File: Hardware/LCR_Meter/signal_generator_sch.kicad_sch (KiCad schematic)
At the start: 0 parts

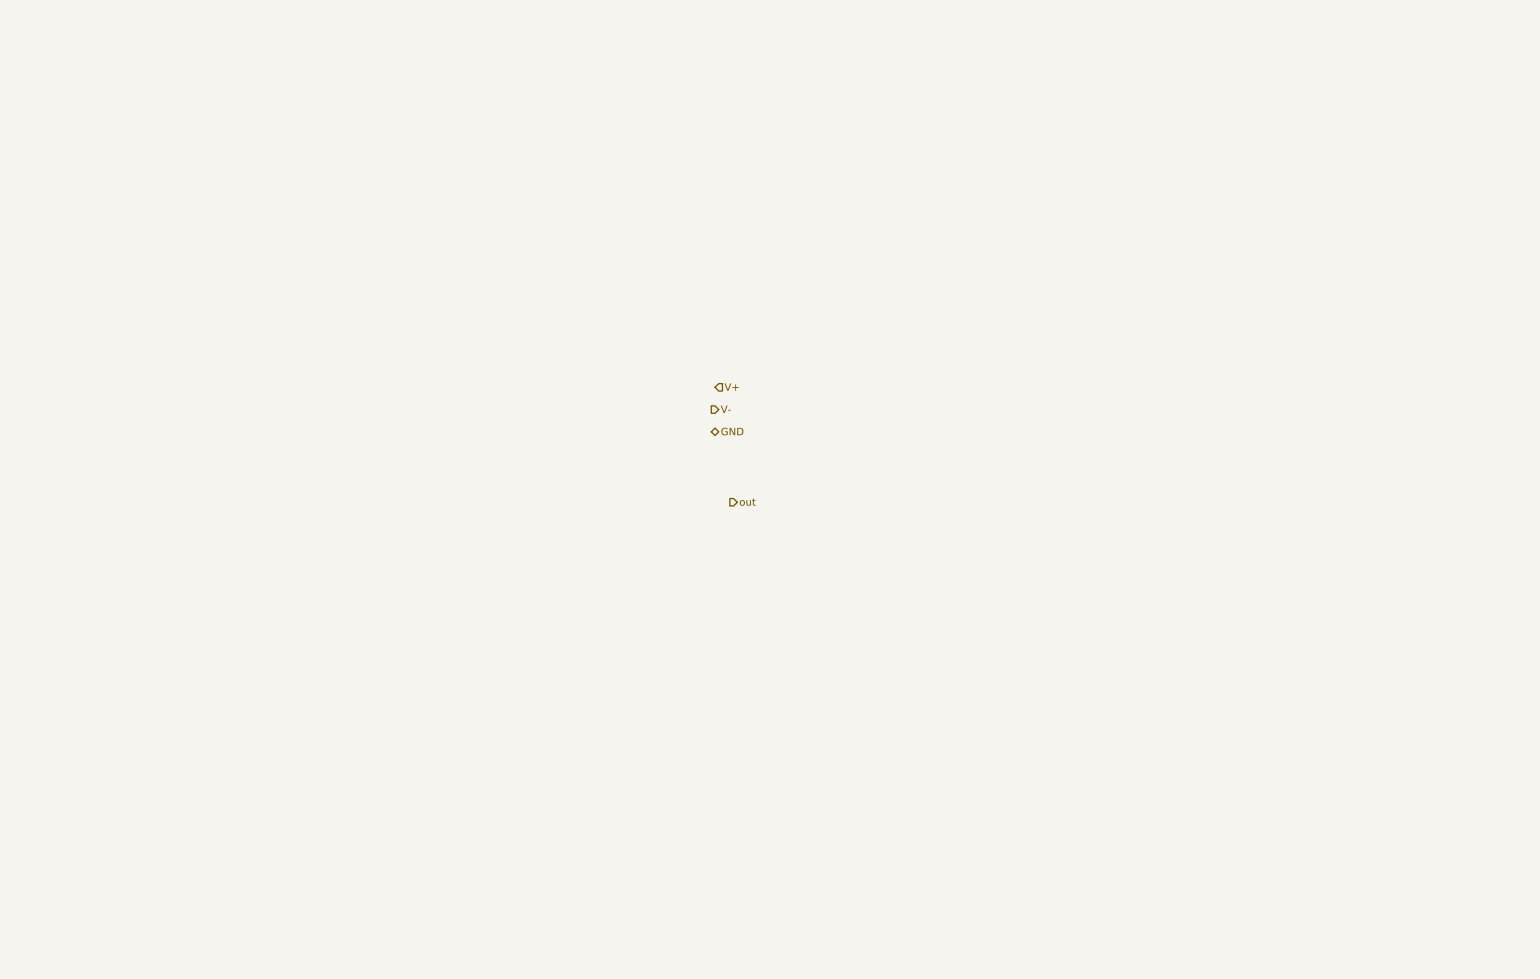
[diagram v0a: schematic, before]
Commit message: work on signal generator
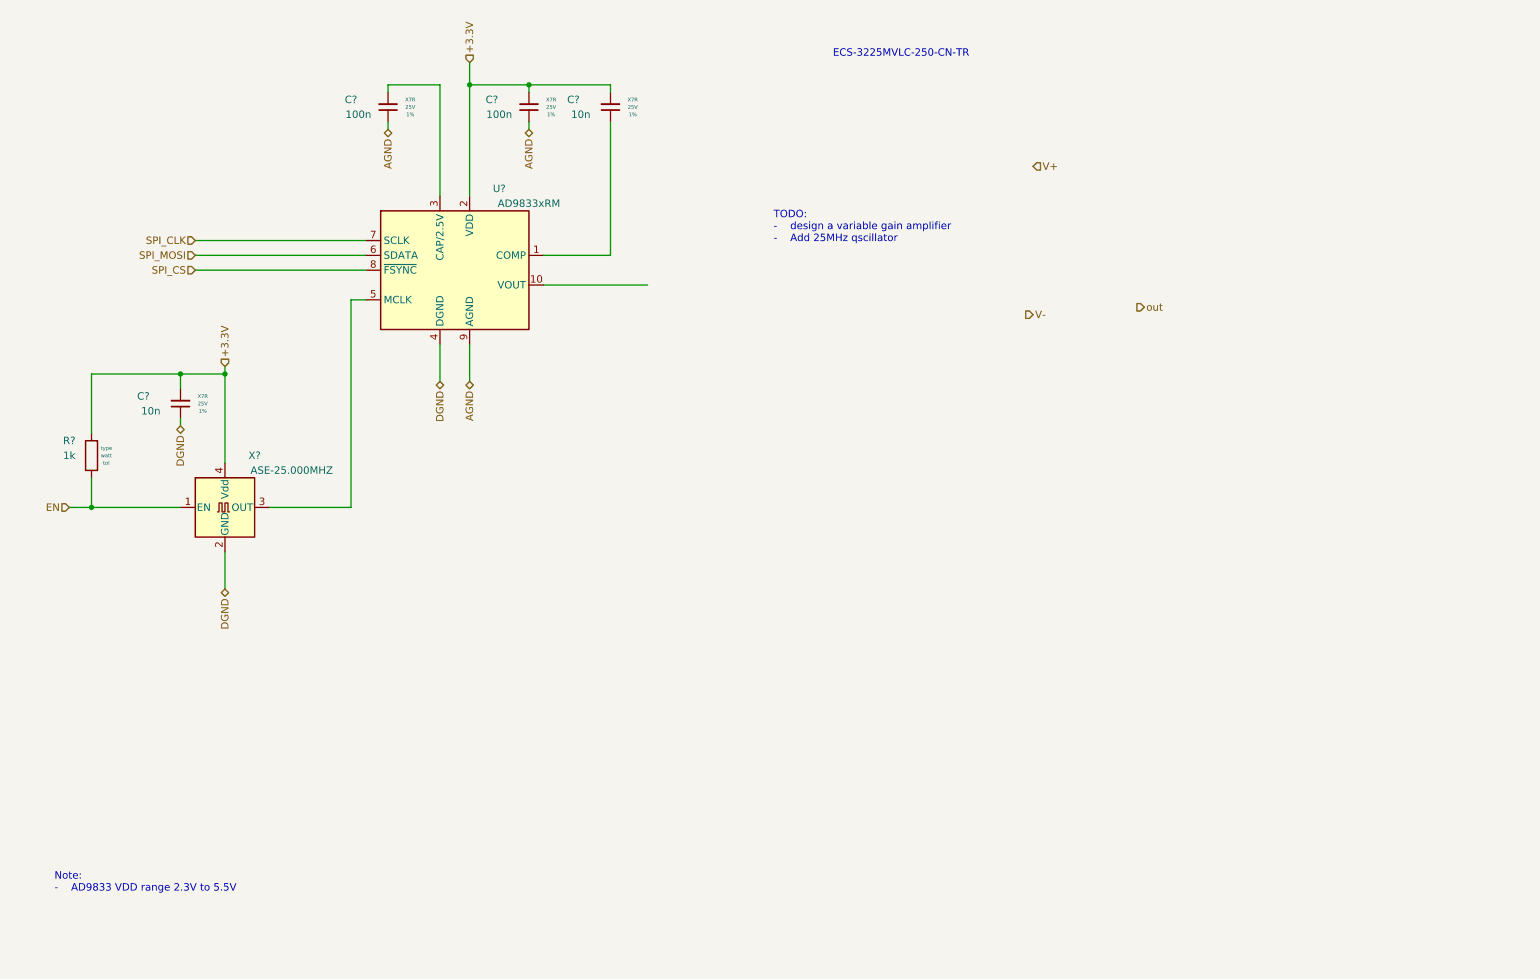
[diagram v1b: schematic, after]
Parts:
- added C? (x2): 100n, Capacitor_SMD:C_0805_2012Metric_Pad1.18x1.45mm_HandSolder, symbol 010_SMD_Capacitors:C_0805_hs
- added C? (x2): 10n, Capacitor_SMD:C_0805_2012Metric_Pad1.18x1.45mm_HandSolder, symbol 010_SMD_Capacitors:C_0805_hs
- added R?: 1k, Resistor_SMD:R_1206_3216Metric, symbol 000_SMD_Resitors:R_1206
- added U?: AD9833xRM, Package_SO:MSOP-10_3x3mm_P0.5mm, symbol Interface:AD9833xRM
- added X?: ASE-25.000MHZ, Oscillator:Oscillator_SMD_Abracon_ASE-4Pin_3.2x2.5mm, symbol Oscillator:ASE-xxxMHz
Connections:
- new net: C?.1, U?.1 (COMP)
- new net: C?.2, U?.3 (CAP/2.5V)
- new net: U?.5 (MCLK), X?.3 (OUT)
- new net +3.3V: C?.2, C?.2, C?.2, R?.2, U?.2 (VDD), X?.4 (Vdd)
- new net AGND: C?.1, C?.1, U?.9 (AGND)
- new net DGND: C?.1, U?.4 (DGND), X?.2 (GND)
- new net EN: R?.1, X?.1 (EN)
- new net SPI_CLK: U?.7 (SCLK)
- new net SPI_CS: U?.8 (~{FSYNC})
- new net SPI_MOSI: U?.6 (SDATA)
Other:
- note added: "ECS-3225MVLC-250-CN-TR"
- note added: "Note: - AD9833 VDD range 2.3V to 5.5V"
- note added: "TODO: - design a variable gain amplifier - Add 25MHz qscillator"

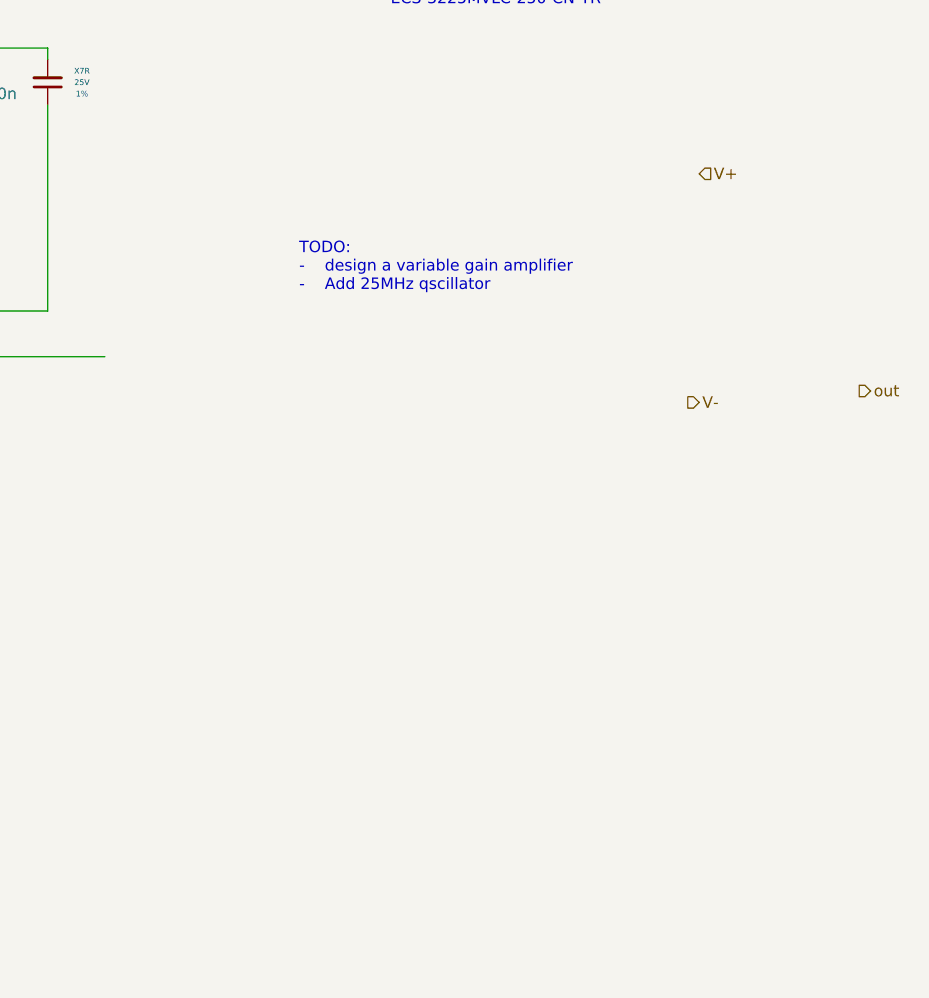
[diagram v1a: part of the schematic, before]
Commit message: work on signal generator signal buffer
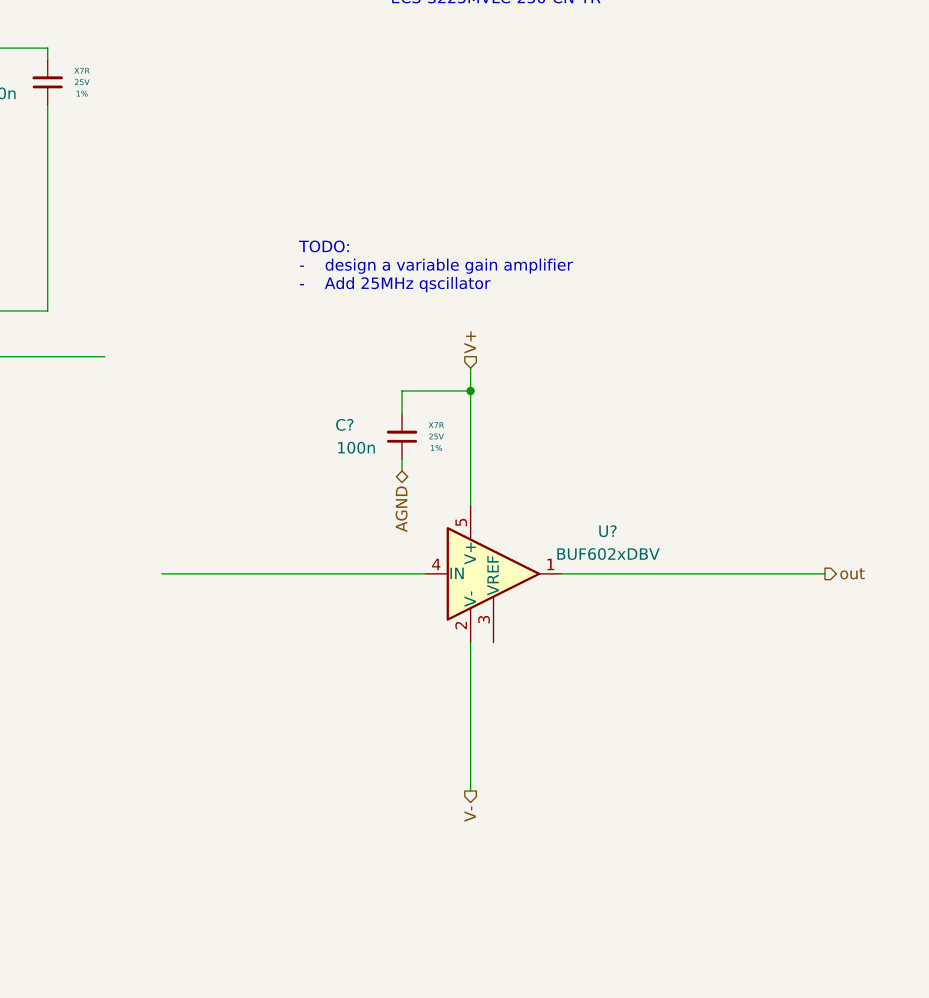
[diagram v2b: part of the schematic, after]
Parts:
- added C?: 100n, Capacitor_SMD:C_0805_2012Metric_Pad1.18x1.45mm_HandSolder, symbol 010_SMD_Capacitors:C_0805_hs
- added U?: BUF602xDBV, Package_TO_SOT_SMD:SOT-23-5, symbol Amplifier_Buffer:BUF602xDBV
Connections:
- net AGND: now also C?.1
- net V+: now also C?.2, U?.5 (V+)
- net V-: now also U?.2 (V-)
- net out: now also U?.1
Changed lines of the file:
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@@
 (kicad_sch (version 20211123) (generator eeschema)
   (paper "A4")
+  (junction (at 171.45 77.47) (diameter 0) (color 0 0 0 0)
+  )
   (junction (at 50.8 88.9) (diameter 0) (color 0 0 0 0)
   )
@@
     (stroke (width 0) (type default) (color 0 0 0 0))
   )
+  (wire (pts (xy 163.83 85.09) (xy 163.83 86.36))
+    (stroke (width 0) (type default) (color 0 0 0 0))
+  )
+  (wire (pts (xy 163.83 77.47) (xy 171.45 77.47))
+    (stroke (width 0) (type default) (color 0 0 0 0))
+  )
   (wire (pts (xy 50.8 111.76) (xy 35.56 111.76))
     (stroke (width 0) (type default) (color 0 0 0 0))
@@
     (stroke (width 0) (type default) (color 0 0 0 0))
   )
+  (wire (pts (xy 137.16 97.79) (xy 166.37 97.79))
+    (stroke (width 0) (type default) (color 0 0 0 0))
+  )
+  (wire (pts (xy 163.83 80.01) (xy 163.83 77.47))
+    (stroke (width 0) (type default) (color 0 0 0 0))
+  )
   (wire (pts (xy 58.42 119.38) (xy 58.42 125.73))
     (stroke (width 0) (type default) (color 0 0 0 0))
@@
     (stroke (width 0) (type default) (color 0 0 0 0))
   )
+  (wire (pts (xy 171.45 121.92) (xy 171.45 105.41))
+    (stroke (width 0) (type default) (color 0 0 0 0))
+  )
   (wire (pts (xy 95.25 39.37) (xy 86.36 39.37))
     (stroke (width 0) (type default) (color 0 0 0 0))
@@
     (stroke (width 0) (type default) (color 0 0 0 0))
   )
+  (wire (pts (xy 181.61 97.79) (xy 210.82 97.79))
+    (stroke (width 0) (type default) (color 0 0 0 0))
+  )
   (wire (pts (xy 50.8 88.9) (xy 50.8 91.44))
     (stroke (width 0) (type default) (color 0 0 0 0))
@@
     (stroke (width 0) (type default) (color 0 0 0 0))
   )
+  (wire (pts (xy 171.45 74.93) (xy 171.45 77.47))
+    (stroke (width 0) (type default) (color 0 0 0 0))
+  )
   (wire (pts (xy 58.42 87.63) (xy 58.42 88.9))
     (stroke (width 0) (type default) (color 0 0 0 0))
   )
   (wire (pts (xy 100.33 35.56) (xy 100.33 39.37))
+    (stroke (width 0) (type default) (color 0 0 0 0))
+  )
+  (wire (pts (xy 171.45 77.47) (xy 171.45 90.17))
     (stroke (width 0) (type default) (color 0 0 0 0))
   )
@@
     (effects (font (size 1.27 1.27)) (justify left bottom))
   )
-  (hierarchical_label "V-" (shape output) (at 195.58 78.74 0)
+  (hierarchical_label "V-" (shape output) (at 171.45 121.92 270)
+    (effects (font (size 1.27 1.27)) (justify right))
+  )
+  (hierarchical_label "DGND" (shape bidirectional) (at 95.25 90.17 270)
+    (effects (font (size 1.27 1.27)) (justify right))
+  )
+  (hierarchical_label "AGND" (shape bidirectional) (at 86.36 46.99 270)
+    (effects (font (size 1.27 1.27)) (justify right))
+  )
+  (hierarchical_label "AGND" (shape bidirectional) (at 110.49 46.99 270)
+    (effects (font (size 1.27 1.27)) (justify right))
+  )
+  (hierarchical_label "DGND" (shape bidirectional) (at 50.8 97.79 270)
+    (effects (font (size 1.27 1.27)) (justify right))
+  )
+  (hierarchical_label "out" (shape output) (at 210.82 97.79 0)
     (effects (font (size 1.27 1.27)) (justify left))
   )
-  (hierarchical_label "DGND" (shape bidirectional) (at 95.25 90.17 270)
-    (effects (font (size 1.27 1.27)) (justify right))
-  )
-  (hierarchical_label "AGND" (shape bidirectional) (at 86.36 46.99 270)
-    (effects (font (size 1.27 1.27)) (justify right))
-  )
-  (hierarchical_label "AGND" (shape bidirectional) (at 110.49 46.99 270)
-    (effects (font (size 1.27 1.27)) (justify right))
-  )
-  (hierarchical_label "DGND" (shape bidirectional) (at 50.8 97.79 270)
-    (effects (font (size 1.27 1.27)) (justify right))
-  )
-  (hierarchical_label "out" (shape output) (at 214.63 77.47 0)
-    (effects (font (size 1.27 1.27)) (justify left))
-  )
   (hierarchical_label "DGND" (shape bidirectional) (at 58.42 125.73 270)
     (effects (font (size 1.27 1.27)) (justify right))
@@
   )
   (hierarchical_label "EN" (shape input) (at 31.75 111.76 180)
+    (effects (font (size 1.27 1.27)) (justify right))
+  )
+  (hierarchical_label "AGND" (shape bidirectional) (at 163.83 86.36 270)
     (effects (font (size 1.27 1.27)) (justify right))
   )
@@
     (effects (font (size 1.27 1.27)) (justify left))
   )
-  (hierarchical_label "V+" (shape input) (at 196.85 53.34 0)
+  (hierarchical_label "V+" (shape input) (at 171.45 74.93 90)
     (effects (font (size 1.27 1.27)) (justify left))
   )
@@
   (hierarchical_label "AGND" (shape bidirectional) (at 100.33 90.17 270)
     (effects (font (size 1.27 1.27)) (justify right))
+  )
+  (symbol (lib_id "Amplifier_Buffer:BUF602xDBV") (at 173.99 97.79 0) (unit 1)
+    (in_bom yes) (on_board yes) (fields_autoplaced)
+    (property "Reference" "U?" (id 0) (at 186.69 93.091 0))
+    (property "Value" "BUF602xDBV" (id 1) (at 186.69 95.631 0))
+    (property "Footprint" "Package_TO_SOT_SMD:SOT-23-5" (id 2) (at 173.99 105.41 0)
+      (effects (font (size 1.27 1.27)) hide)
+    )
+    (property "Datasheet" "http://www.ti.com/lit/ds/symlink/buf602.pdf" (id 3) (at 173.99 97.79 0)
+      (effects (font (size 1.27 1.27)) hide)
+    )
+    (pin "1")
+    (pin "2")
+    (pin "3")
+    (pin "4")
+    (pin "5")
   )
   (symbol (lib_id "Interface:AD9833xRM") (at 97.79 71.12 0) (unit 1)
@@
       (effects (font (size 1.27 1.27)) hide)
     )
+    (pin "1")
+    (pin "2")
+  )
+  (symbol (lib_id "010_SMD_Capacitors:C_0805_hs") (at 163.83 82.55 180) (unit 1)
+    (in_bom yes) (on_board yes)
+    (property "Reference" "C?" (id 0) (at 157.48 81.28 0))
+    (property "Value" "100n" (id 1) (at 158.75 83.82 0))
+    (property "Footprint" "Capacitor_SMD:C_0805_2012Metric_Pad1.18x1.45mm_HandSolder" (id 2) (at 161.925 69.85 0)
+      (effects (font (size 1.27 1.27)) hide)
+    )
+    (property "Datasheet" "ds" (id 3) (at 139.7 86.36 0)
+      (effects (font (size 1.27 1.27)) hide)
+    )
+    (property "type" "X7R" (id 4) (at 167.64 81.28 0)
+      (effects (font (size 0.635 0.635)))
+    )
+    (property "voltage" "25V" (id 5) (at 167.64 82.55 0)
+      (effects (font (size 0.635 0.635)))
+    )
+    (property "tol" "1%" (id 6) (at 167.64 83.82 0)
+      (effects (font (size 0.635 0.635)))
+    )
+    (property "man" "man" (id 7) (at 140.97 97.79 0)
+      (effects (font (size 1.27 1.27)) hide)
+    )
+    (property "man_no" "man_no" (id 8) (at 142.24 95.25 0)
+      (effects (font (size 1.27 1.27)) hide)
+    )
+    (property "dist" "dist" (id 9) (at 140.97 91.44 0)
+      (effects (font (size 1.27 1.27)) hide)
+    )
+    (property "dist_no" "dist_no" (id 10) (at 142.24 88.9 0)
+      (effects (font (size 1.27 1.27)) hide)
+    )
